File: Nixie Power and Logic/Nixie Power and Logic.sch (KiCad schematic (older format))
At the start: 54 parts, among them J1 Barrel_Jack, J10 Conn_01x20_Female, J11 Conn_01x20_Female, J12 Conn_01x20_Female, J13 LED Data, J2 Conn_01x02_Female, J3 Conn_01x02_Female, J4 Conn_01x02_Female, J5 Conn_01x02_Female, J6 Conn_01x02_Female, J7 Conn_01x02_Female, J8 Programming, J9 RTC, Q1 IRF740, Q2 MPSA92, Q3 BC547, SW1 SW_SPST, SW2 SW_SPST, SW3 Rotary_Encoder_EN11, SW4 Rotary_Encoder_EN11, SW5 Rotary_Encoder_EN11, SW6 SW_Reset, U1 ATmega168PA-PU, U10 74141, U11 L7805, U12 NE555, U2 74HC595, U3 74HC595, U4 74HC595, U5 74141, U6 74141, U7 74141, U8 74141, U9 74141, Y1 20MHz

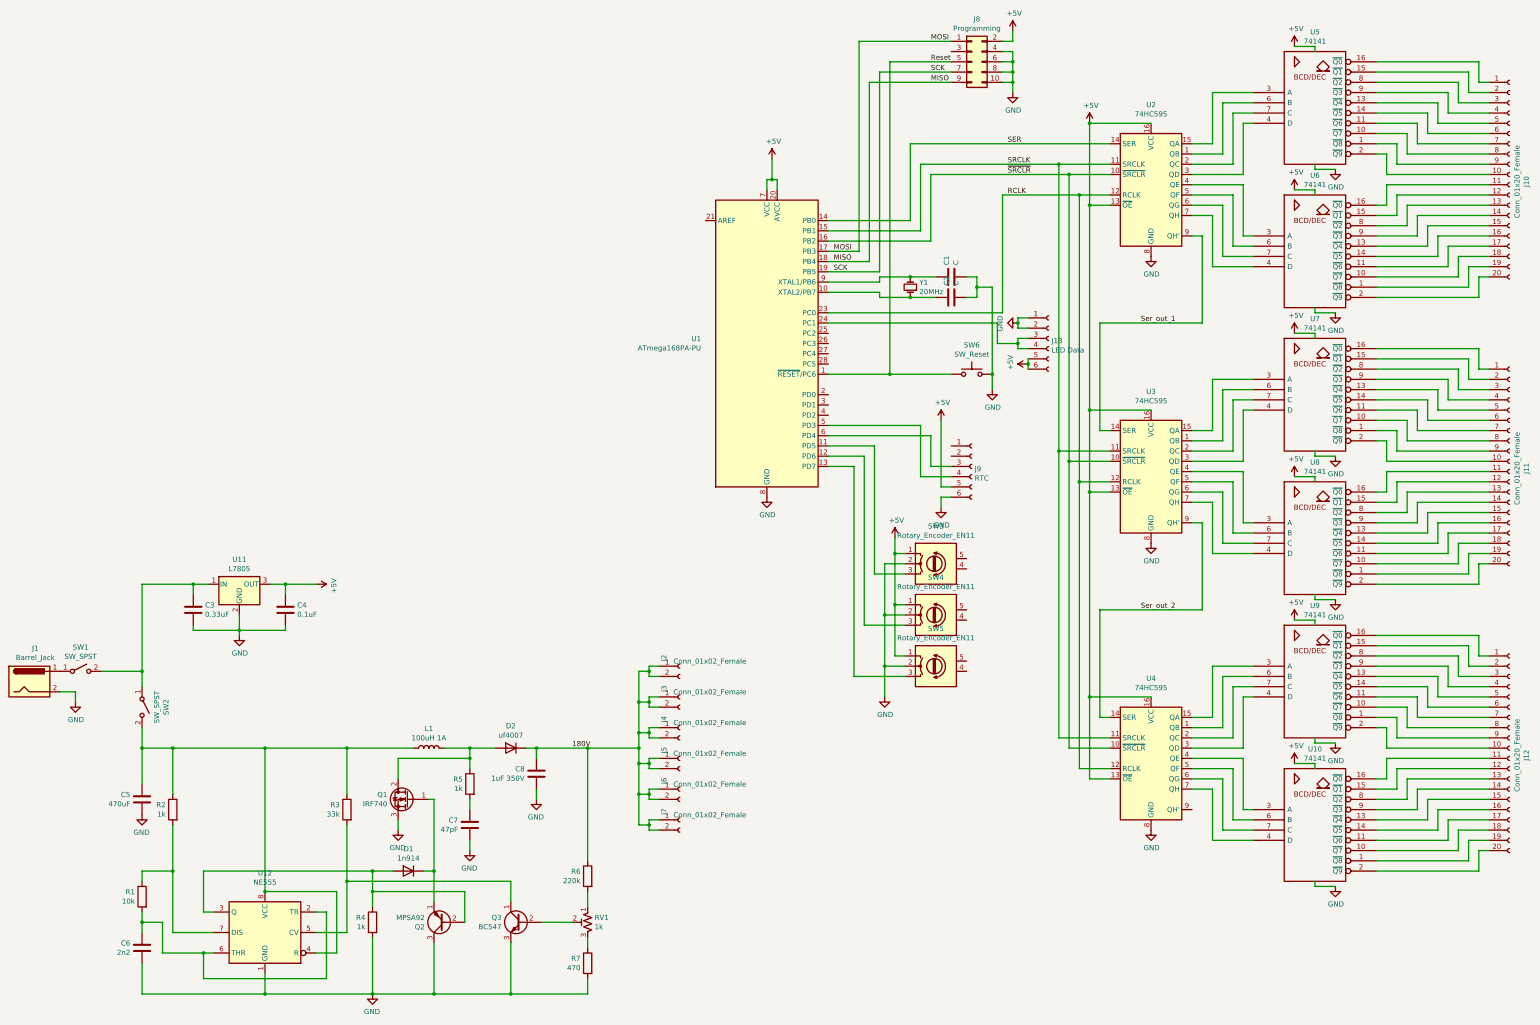
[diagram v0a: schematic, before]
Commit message: Final V1.0 design. Different sized boards for top and bottom layer. Goal for v2.0 is to have matching top and bottom pcbas
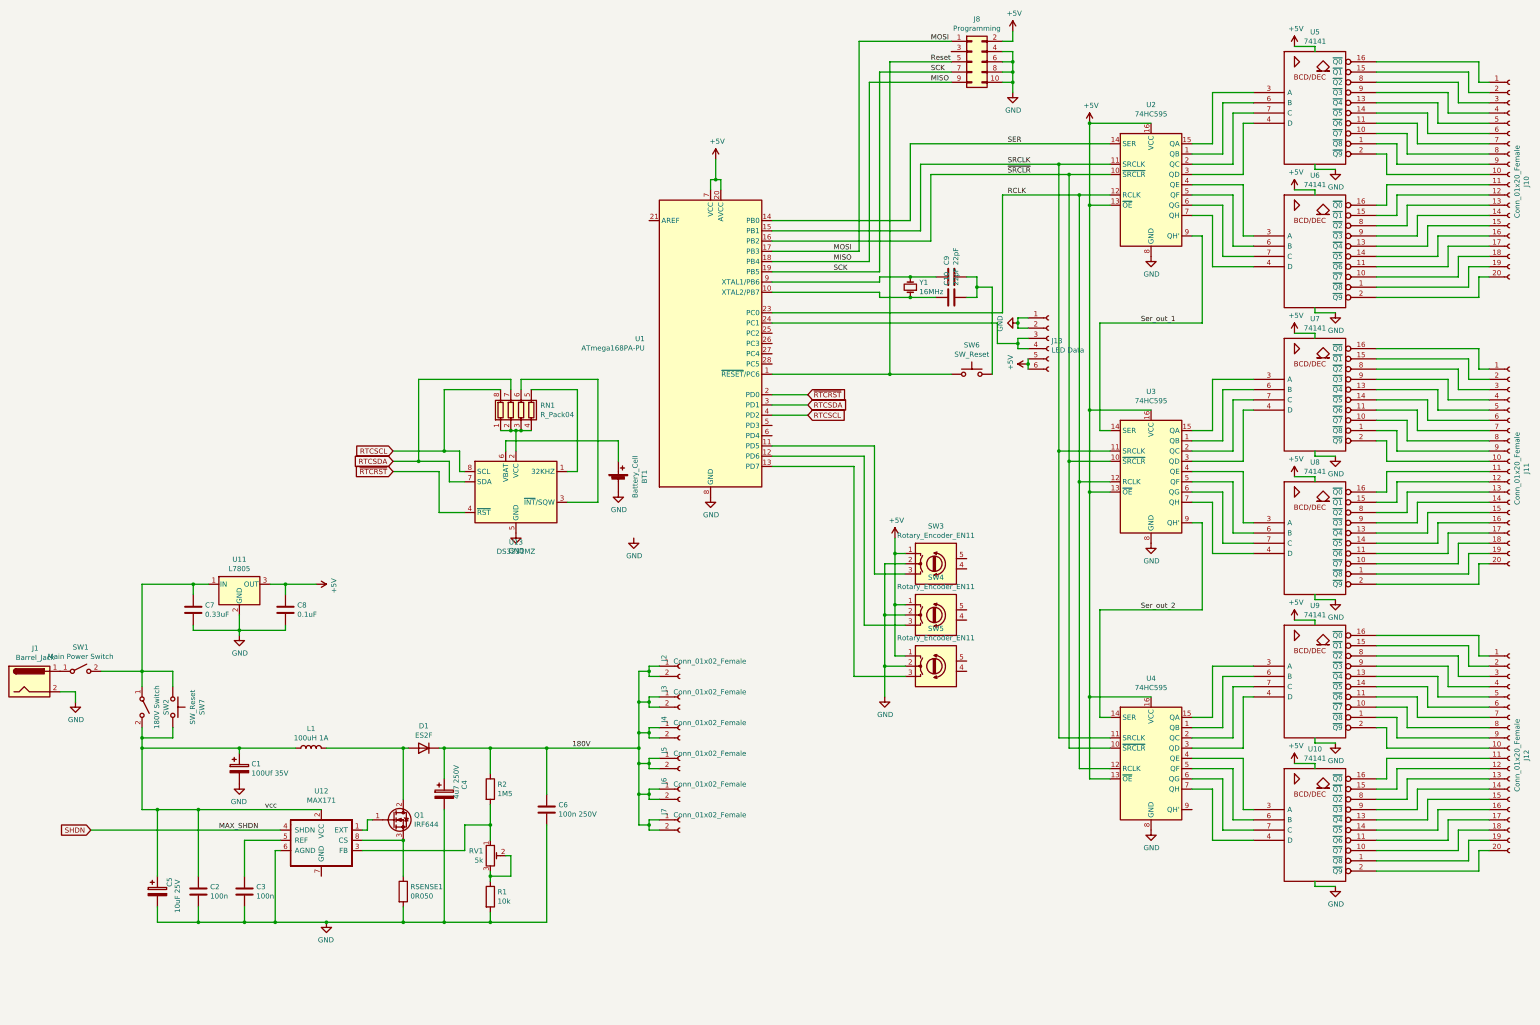
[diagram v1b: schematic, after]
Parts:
- removed C5: 470uF, Capacitor_THT:CP_Radial_D10.0mm_P5.00mm, symbol Device:C
- removed C7: 47pF, Capacitor_SMD:C_0603_1608Metric_Pad1.05x0.95mm_HandSolder, symbol Device:C
- removed C8: 1uF 350V, Capacitor_THT:CP_Radial_D6.3mm_P2.50mm, symbol Device:C
- removed D2: uf4007, Diode_THT:D_DO-41_SOD81_P10.16mm_Horizontal, symbol Device:D
- removed J9: RTC, Connector_PinHeader_2.54mm:PinHeader_1x06_P2.54mm_Horizontal, symbol Connector:Conn_01x06_Female
- removed Q1: IRF740, Package_TO_SOT_THT:TO-220-3_Horizontal_TabDown, symbol Transistor_FET:IRF740
- removed Q2: MPSA92, Package_TO_SOT_THT:TO-92_Inline, symbol Transistor_BJT:MPSA92
- removed Q3: BC547, Package_TO_SOT_THT:TO-92_Inline, symbol Transistor_BJT:BC547
- removed R3: 33k, Resistor_SMD:R_0603_1608Metric_Pad1.05x0.95mm_HandSolder, symbol Device:R
- removed R4, R5: 1k, Resistor_SMD:R_0603_1608Metric_Pad1.05x0.95mm_HandSolder, symbol Device:R
- removed R6: 220k, Resistor_SMD:R_1206_3216Metric_Pad1.42x1.75mm_HandSolder, symbol Device:R
- removed R7: 470, Resistor_SMD:R_1206_3216Metric_Pad1.42x1.75mm_HandSolder, symbol Device:R
- removed RV1: 1k, Potentiometer_THT:Potentiometer_Bourns_3386F_Vertical, symbol Device:R_POT_TRIM_US
- removed U12: NE555, Package_DIP:SMDIP-8_W7.62mm, symbol Timer:NE555
- added BT1: Battery_Cell, Battery:BatteryHolder_Keystone_3000_1x12mm, symbol Device:Battery_Cell
- added C1: 100Uf 35V, Capacitor_Tantalum_SMD:CP_EIA-7343-31_Kemet-D_Pad2.25x2.55mm_HandSolder, symbol Device:CP
- added C2, C3: 100n, Capacitor_SMD:C_0805_2012Metric_Pad1.15x1.40mm_HandSolder, symbol Device:C
- added C4: 4u7 250V, Capacitor_SMD:CP_Elec_10x14.3, symbol Device:CP
- added C5: 10uF 25V, Capacitor_Tantalum_SMD:CP_EIA-7343-31_Kemet-D_Pad2.25x2.55mm_HandSolder, symbol Device:CP
- added Q1: IRF644, Package_TO_SOT_THT:TO-220-3_Vertical, symbol Transistor_FET:BUZ11
- added RN1: R_Pack04, Resistor_SMD:R_Array_Convex_4x0603, symbol Device:R_Pack04
- added RSENSE1: 0R050, Resistor_SMD:R_2010_5025Metric_Pad1.52x2.65mm_HandSolder, symbol Device:R
- added RV1: 5k, Potentiometer_SMD:Potentiometer_Bourns_3214W_Vertical, symbol Device_Eric:R_POT_TRIM
- added SW7: SW_Reset, Connector_Wire:SolderWirePad_1x02_P3.81mm_Drill1mm, symbol Switch:SW_Push
- added U12: MAX171, Nixie Power and Logic:SOIC−8-NARROW, symbol Device_Eric:MAX171
- added U13: DS3231MZ, Package_SO:SOIC-8_3.9x4.9mm_P1.27mm, symbol Timer_RTC:DS3231MZ
- C10: renamed from C2; value C -> 22pF
- C6: value 2n2 -> 100n 250V; footprint Capacitor_SMD:C_0402_1005Metric -> Capacitor_SMD:C_2220_5650Metric_Pad1.97x5.40mm_HandSolder
- C9: renamed from C1; value C -> 22pF
- D1: value 1n914 -> ES2F; footprint Diode_THT:D_A-405_P7.62mm_Horizontal -> Nixie Power and Logic:D_SOD-214AA
- J13: footprint Connector_PinHeader_2.54mm:PinHeader_1x06_P2.54mm_Vertical -> Connector_PinSocket_2.54mm:PinSocket_1x06_P2.54mm_Vertical_SMD_Pin1Left
- L1: footprint Inductor_THT:L_Radial_D9.5mm_P5.00mm_Fastron_07HVP -> Inductor_SMD:L_Bourns_SDR1806
- R1: footprint Resistor_SMD:R_0603_1608Metric_Pad1.05x0.95mm_HandSolder -> Resistor_SMD:R_0805_2012Metric_Pad1.15x1.40mm_HandSolder
- R2: value 1k -> 1M5; footprint Resistor_SMD:R_0603_1608Metric_Pad1.05x0.95mm_HandSolder -> Resistor_SMD:R_2512_6332Metric_Pad1.52x3.35mm_HandSolder
- SW1: value SW_SPST -> Main Power Switch; footprint Potentiometer_THT:Potentiometer_Bourns_3386P_Vertical -> Connector_Wire:SolderWirePad_1x02_P3.81mm_Drill1mm
- SW2: value SW_SPST -> 180V Switch; footprint Potentiometer_THT:Potentiometer_Piher_PT-6-H_Horizontal -> Connector_Wire:SolderWirePad_1x02_P3.81mm_Drill1mm
- Y1: value 20MHz -> 16MHz
- renumbered C3 to C7, C4 to C8
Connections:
- net 180V: now also C6.1, D1.1 (K), R2.1, C4.1
- net GND: now also R1.2, BT1.2 (-), C1.2, C2.2, C3.2, C4.2, C5.2, RSENSE1.2, U12.6 (AGND), U13.5 (GND); no longer C10.2, C9.2, SW6.2
- net at C7.1, SW1.2 (B), SW2.1 (A)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: now also SW7.1
- net vcc: now reaches L1.2, SW2.2 (B)
- net vcc: now also C1.1, C2.1, C5.1, SW7.2, U12.2 (VCC); no longer R2.1
- net ~RTCRST: now reaches U1.2 (PD0)
- net ~RTCRST: now also U13.4 (~RST)
- net RTCSDA: now reaches U1.3 (PD1)
- net RTCSDA: now also RN1.7 (R2.2), U13.7 (SDA)
- net RTCSCL: now reaches U1.4 (PD2)
- net RTCSCL: now also RN1.8 (R1.2), U13.8 (SCL)
- net at D1.2 (A): now also L1.1, Q1.2 (D)
- net at R2.2: now also RV1.1, U12.3 (FB); no longer R1.1
- new net: C10.2, C9.2, SW6.2
- new net: Q1.1 (G), U12.1 (EXT)
- new net: C3.1, U12.5 (REF)
- new net: Q1.3 (S), RSENSE1.1, U12.8 (CS)
- new net: R1.1, RV1.2, RV1.3
- new net: RN1.5 (R4.2), U13.1 (32KHZ)
- new net: RN1.1 (R1.1), RN1.2 (R2.1), RN1.3 (R3.1), RN1.4 (R4.1), U13.2 (VCC)
- new net: RN1.6 (R3.2), U13.3 (~INT~/SQW)
- new net: BT1.1 (+), U13.6 (VBAT)
- new net SHDN: U12.4 (SHDN)
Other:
- moved on the sheet: L1, U1
